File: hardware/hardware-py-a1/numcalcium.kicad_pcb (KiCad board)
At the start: 2 copper layers, 77.6 x 161.1 mm, 143 parts, among them J1 Conn_01x14_Socket, J2 Conn_01x14_Socket, J3 LCD_socket, J4 Micro_SD_Card_Det2, J5 AudioJack4, J6 USB_C_Receptacle_USB2.0_16P, J7 Conn_02x08_Odd_Even, Q1 AO3401A, Q2 BSS138, Q3 AO3401A, Q5 AO4953A, Q6 BSS138, Q8 BSS138, Q9 BSS138, SW1 SW_Push, SW10 SW_Push, SW11 SW_Push, SW12 SW_Push, SW13 SW_Push, SW14 SW_Push, SW15 SW_Push, SW16 SW_Push, SW17 SW_Push, SW18 SW_Push, SW19 SW_Push, SW2 SW_Push, SW20 SW_Push, SW21 Encoder, SW22 SW_Push, SW3 SW_Push, SW4 SW_Push, SW5 SW_Push, SW6 SW_Push, SW7 SW_Push, SW8 SW_Push, SW9 SW_Push, U1 LTC4054, U2 STI3411A, U3 74HC595, U4 ESP32-S3-WROOM-1, U5 XC6206PxxxMR

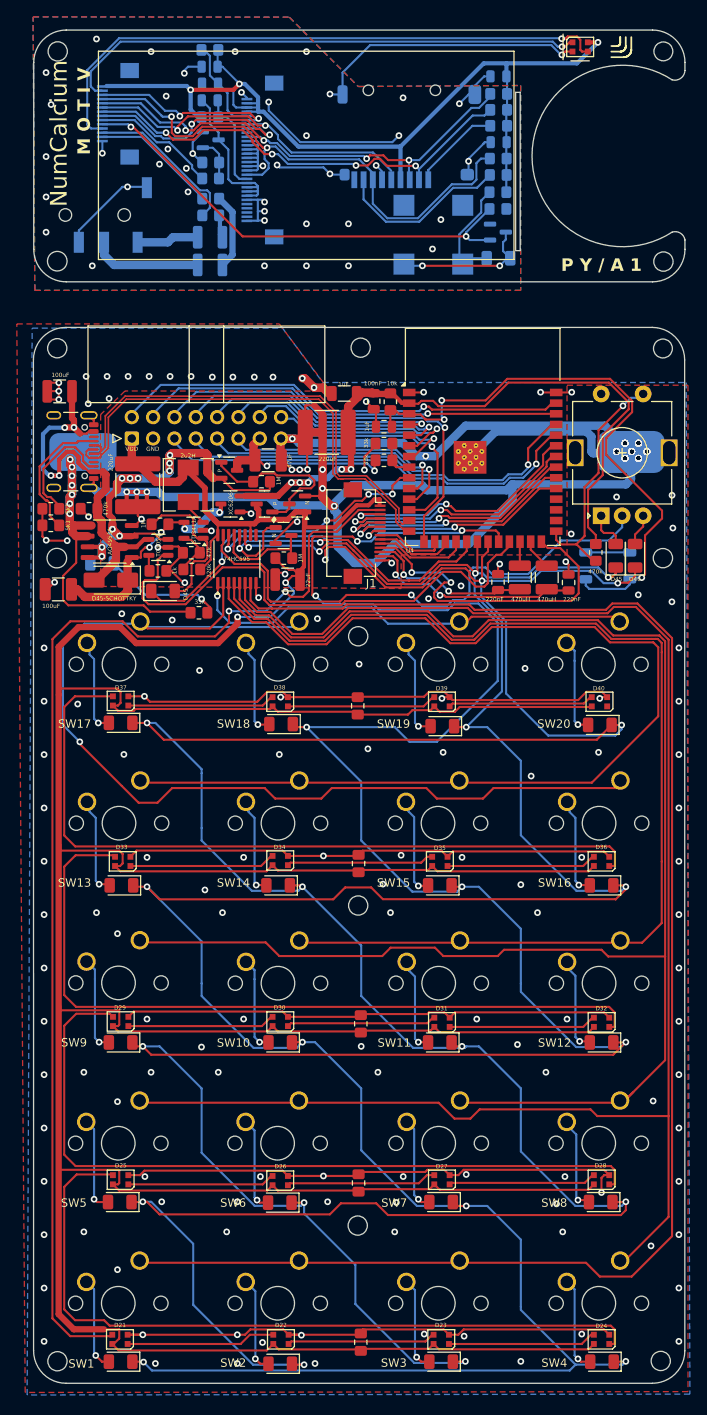
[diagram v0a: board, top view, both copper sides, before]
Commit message: hw: passives values simpler, tantlum caps, silkscreen tweaks
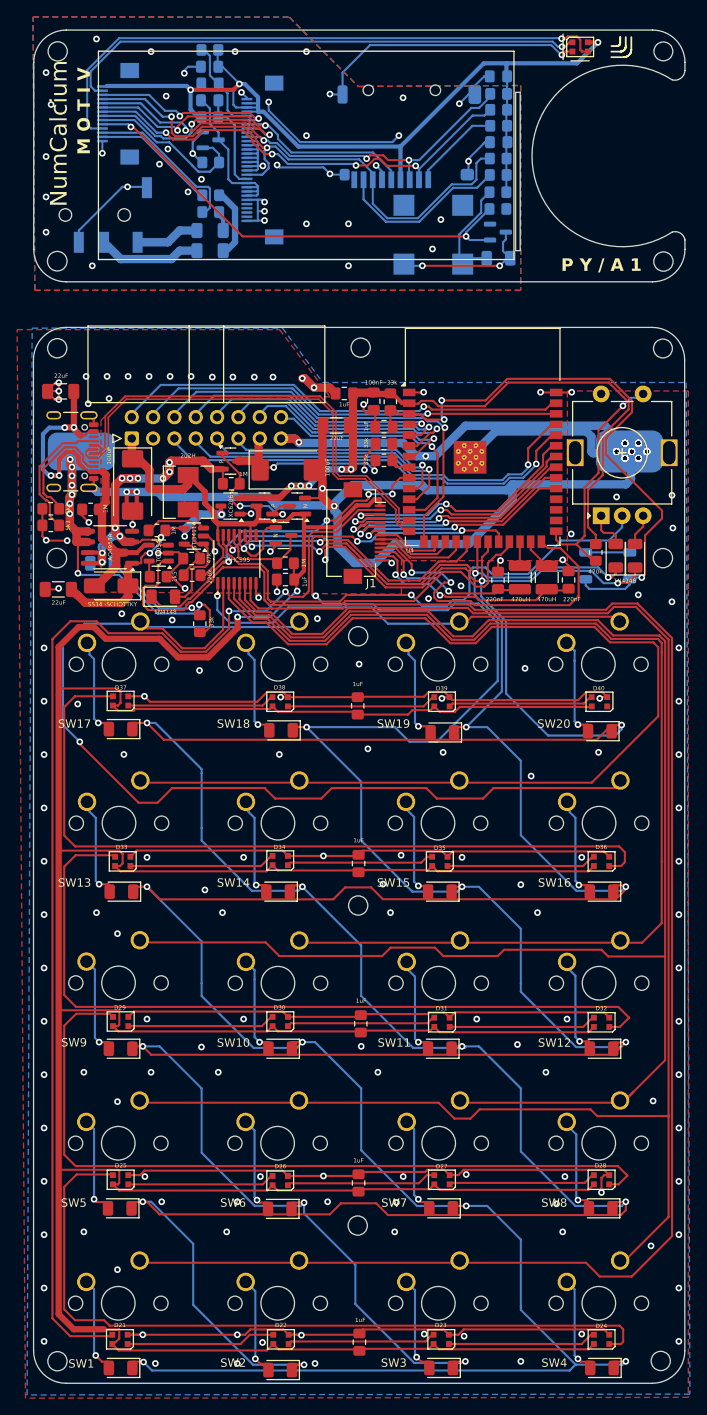
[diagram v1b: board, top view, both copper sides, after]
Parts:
- removed R20: 1k, Resistor_SMD:R_0805_2012Metric_Pad1.20x1.40mm_HandSolder
- C1: value 100uF -> 22u; footprint Capacitor_SMD:C_1210_3225Metric -> Capacitor_SMD:C_1206_3216Metric_Pad1.33x1.80mm_HandSolder
- C10, C20, C21, C4, C9: footprint Capacitor_SMD:C_0805_2012Metric -> Capacitor_SMD:C_0805_2012Metric_Pad1.18x1.45mm_HandSolder
- C11, C8: value 100n -> 220n; footprint Capacitor_SMD:C_0805_2012Metric -> Capacitor_SMD:C_0805_2012Metric_Pad1.18x1.45mm_HandSolder
- C12, C13: footprint Capacitor_SMD:C_1210_3225Metric -> Capacitor_SMD:C_1206_3216Metric_Pad1.33x1.80mm_HandSolder
- C15: value 10u -> 1u; footprint Capacitor_SMD:C_0805_2012Metric -> Capacitor_SMD:C_0805_2012Metric_Pad1.18x1.45mm_HandSolder
- C2: value 220u -> 100u; footprint Capacitor_SMD:C_2220_5750Metric -> Capacitor_Tantalum_SMD:CP_EIA-7343-31_Kemet-D
- C22: value 100u -> 22u; footprint Capacitor_SMD:C_1210_3225Metric_Pad1.33x2.70mm_HandSolder -> Capacitor_SMD:C_1206_3216Metric_Pad1.33x1.80mm_HandSolder
- C23: value 2u2 -> 1u; footprint Capacitor_SMD:C_0805_2012Metric -> Capacitor_SMD:C_0805_2012Metric_Pad1.18x1.45mm_HandSolder
- C3: value 47u -> 100u; footprint Capacitor_SMD:C_1210_3225Metric_Pad1.33x2.70mm_HandSolder -> Capacitor_Tantalum_SMD:CP_EIA-7343-31_Kemet-D
- C5: value 22u -> 1u; footprint Capacitor_SMD:C_1210_3225Metric -> Capacitor_SMD:C_0805_2012Metric_Pad1.18x1.45mm_HandSolder
- C6: value 220u -> 22u; footprint Capacitor_SMD:C_2220_5750Metric -> Capacitor_SMD:C_1206_3216Metric_Pad1.33x1.80mm_HandSolder
- C7: footprint Capacitor_SMD:C_1206_3216Metric -> Capacitor_SMD:C_0805_2012Metric_Pad1.18x1.45mm_HandSolder
- D1, D10, D11, D12, D13, D14, D15, D16, D17, D18, D19, D2, D20, D3, D4, D42, D44, D45, D46, D5, D6, D7, D8, D9: value D -> 1N4148
- D47: value BAT_REV -> LED
- R14: value 10k -> 33k
- R15, R18: value 100k -> 470k
- R2: value 47 -> 100
- R26: value 470k -> 1M
- R28, R29: value 2k2 -> 1k5
- R4: value 1k -> 1k5
- moved R7 3.61 mm to (23.0, 9.91), turned to 0 degrees
- moved C3 2.44 mm to (29.6, 8.26)
- moved C13 1.70 mm to (20.5, -17.8)
- moved C6 1.40 mm to (35.5, 2.96)
- moved R1 1.30 mm to (19.3, 26.6), turned to 90 degrees
- moved Q1 1.10 mm to (22.9, 7.21)
- moved L1 0.88 mm to (17.9, 10.9)
- moved R3 0.82 mm to (14.2, 15.5)
- moved C12 0.80 mm to (20.5, -20.2)
- moved D1 0.75 mm to (9.87, 115.2)
- moved D10 0.75 mm to (28.9, 77.2)
- moved D11 0.75 mm to (47.9, 77.2)
- moved D12 0.75 mm to (67.1, 77.2)
- moved D13 0.75 mm to (9.97, 58.5)
- moved D14 0.75 mm to (28.6, 58.5)
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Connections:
- net USB+ renamed Net-(U4-USB_D+)
- net USB- renamed Net-(U4-USB_D-)
- Q9 pad 1: Net-(Q9-G) -> /Front/LCD_LED
- R18 pad 1: Net-(Q9-G) -> /Front/LCD_LED
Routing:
- net GND: track 710.0 -> 682.7 mm, vias 312 -> 305
- net /Front/LCD_LED: track 15.0 -> 20.2 mm
- net Net-(Q9-G): track 5.16 -> 0.00 mm
- net Net-(Q1-G): track 20.5 -> 17.2 mm, vias 0 -> 2
- net Net-(U3-QC): track 127.3 -> 130.2 mm
- net Net-(D32-DOUT): track 90.7 -> 93.1 mm
- net Net-(D36-DOUT): track 90.3 -> 92.4 mm
- net Net-(D28-DOUT): track 90.5 -> 92.6 mm
- net /Main/LED_RETURN: track 141.4 -> 143.3 mm
- net Net-(D24-DOUT): track 89.9 -> 91.8 mm
- net #LOW_POWER_REQ: track 39.1 -> 40.9 mm
- net Net-(Q6-D): track 13.5 -> 11.7 mm
- net Net-(Q1-S): track 51.6 -> 50.1 mm
- net VDD_AON: track 82.4 -> 83.8 mm
- net Net-(BT1-+): track 46.5 -> 47.8 mm, vias 7 -> 9
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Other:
- board text added: "1N4148"
- board text added: "1k5"
- board text added: "Battery Reversed"
- board text added: "SS34 -SCHOTTKY"
- board text added: "Unit:"
- board text removed: "100k"
- board text removed: "10k"
- board text removed: "10uF"
- board text removed: "220uF"
- board text removed: "2k2"
- board text removed: "2u2F"
- board text removed: "47R"
- board text removed: "47uF"
- board text removed: "D42"
- board text removed: "D45"
- board text removed: "D45-SCHOTTKY"
- board text removed: "D46"
- board text removed: "GND"
- board text removed: "VDD"

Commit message: hw: fixes for py-a1
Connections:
- C10 pad 2: GND -> /Front/GND
- C11 pad 2: GND -> /Front/GND
- C15 pad 2: GND -> /Front/GND
- C23 pad 2: GND -> /Front/GND
- D41 pad 2: GND -> /Front/GND
- J2 pad 14: GND -> /Front/GND
- J3 pad 1: GND -> /Front/GND
- J3 pad 11: GND -> /Front/GND
- J3 pad 12: GND -> /Front/GND
- J3 pad 13: GND -> /Front/GND
- J3 pad 14: GND -> /Front/GND
- J3 pad 15: GND -> /Front/GND
- J3 pad 16: GND -> /Front/GND
- J3 pad 17: GND -> /Front/GND
- J3 pad 18: GND -> /Front/GND
- J3 pad 25: GND -> /Front/GND
- J3 pad 30: GND -> /Front/GND
- J4 pad 11: GND -> /Front/GND
- J4 pad 6: GND -> /Front/GND
- J5 pad R2: GND -> /Front/GND
- J5 pad S: GND -> /Front/GND
- Q8 pad 2: GND -> /Front/GND
- Q9 pad 2: GND -> /Front/GND
- R18 pad 2: GND -> /Front/GND
- R27 pad 2: GND -> /Front/GND
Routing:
- net /Front/GND: track 0.00 -> 129.6 mm, vias 0 -> 40
- net GND: track 682.7 -> 565.3 mm, vias 305 -> 265
- net IO_D: track 351.4 -> 354.5 mm
- net IO_CK: track 326.1 -> 328.0 mm
- net IO_T: track 281.4 -> 282.2 mm
- added copper zone on B.Cu, net /Front/GND
- added copper zone on F.Cu, net /Front/GND

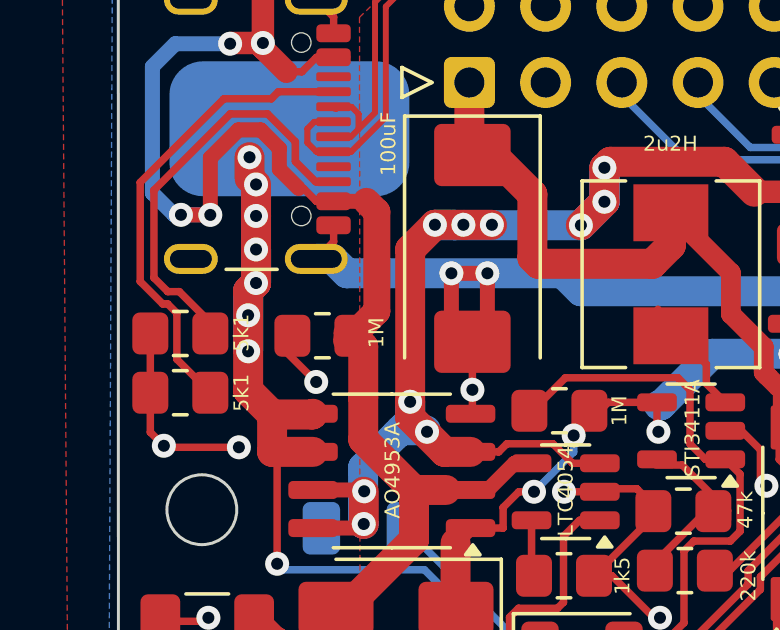
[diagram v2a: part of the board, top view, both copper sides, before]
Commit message: hw: pya1 schematic rearange and post assembly test for inputs
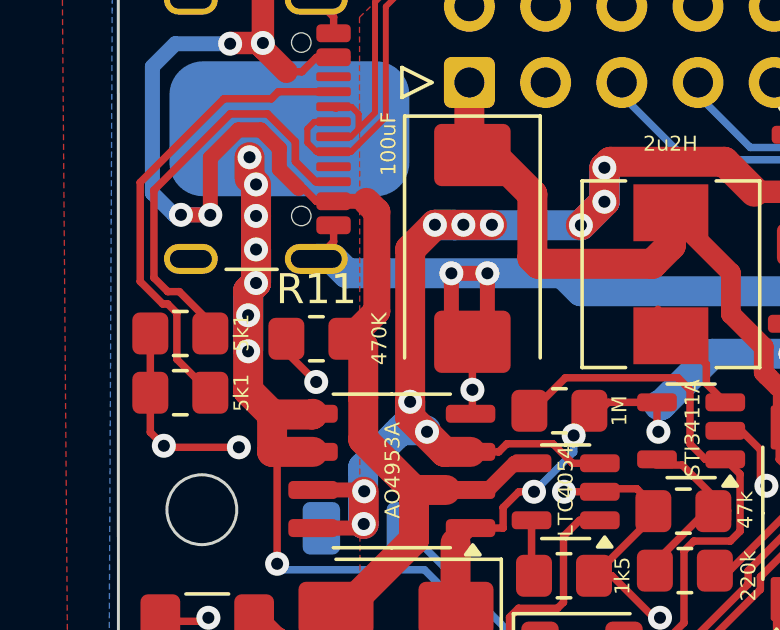
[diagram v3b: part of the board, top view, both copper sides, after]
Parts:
- removed R26: 1M, Resistor_SMD:R_0805_2012Metric_Pad1.20x1.40mm_HandSolder
- added R11: 470k, Resistor_SMD:R_0805_2012Metric_Pad1.20x1.40mm_HandSolder, F.Cu at (6.09, 13.1)
- R19, R2: value 100 -> 22
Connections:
- net Net-(D43-K) renamed VCC_REG
- net Net-(Q1-G) renamed SYSTEM_ON_CTRL
- net Net-(Q1-S) renamed VBAT_CH
- C6 pad 1: VDD_AON -> VDD
- C7 pad 1: VDD_AON -> VDD
- C8 pad 1: VDD_AON -> VDD
- Q3 pad 2: VDD_AON -> VDD
- R12 pad 1: VDD_AON -> VDD
- R14 pad 1: VDD_AON -> VDD
- U4 pad 2: VDD_AON -> VDD
- U5 pad 2: VDD_AON -> VDD
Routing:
- net VDD: track 525.7 -> 609.5 mm, vias 2 -> 7
- net VDD_AON: track 83.8 -> 0.00 mm, vias 5 -> 0
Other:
- board text added: "470K"
- board text removed: "1k"
